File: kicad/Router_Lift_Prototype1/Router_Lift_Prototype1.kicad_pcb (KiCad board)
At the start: 2 copper layers, 143 x 93 mm, 37 parts, among them J1 Conn_01x02, J10 Conn_01x02, J11 Conn_01x04, J2 Conn_01x02, J3 Conn_01x06, J4 Conn_01x06, J5 Conn_01x06, J6 Conn_01x02, J7 Conn_01x02, J8 Conn_01x02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

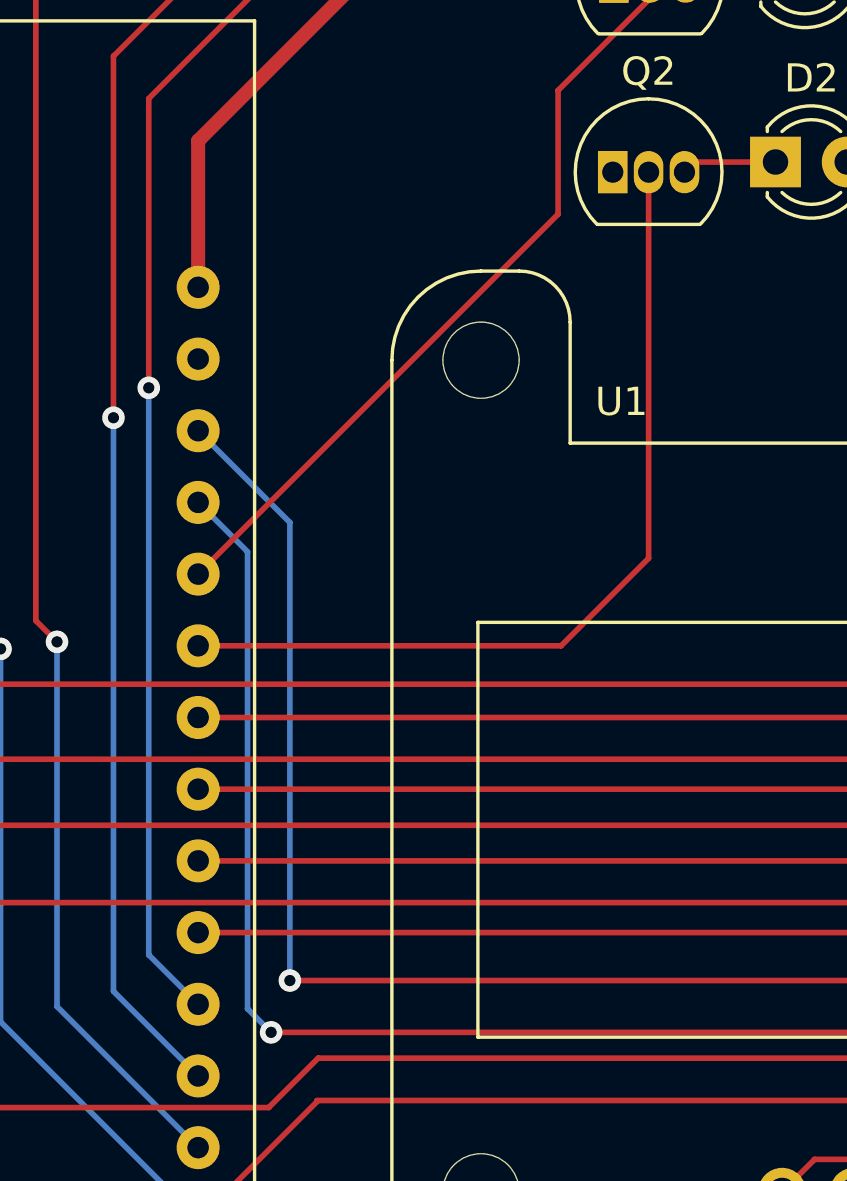
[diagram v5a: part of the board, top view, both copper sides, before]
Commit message: Created the board with DRV8711 Integration
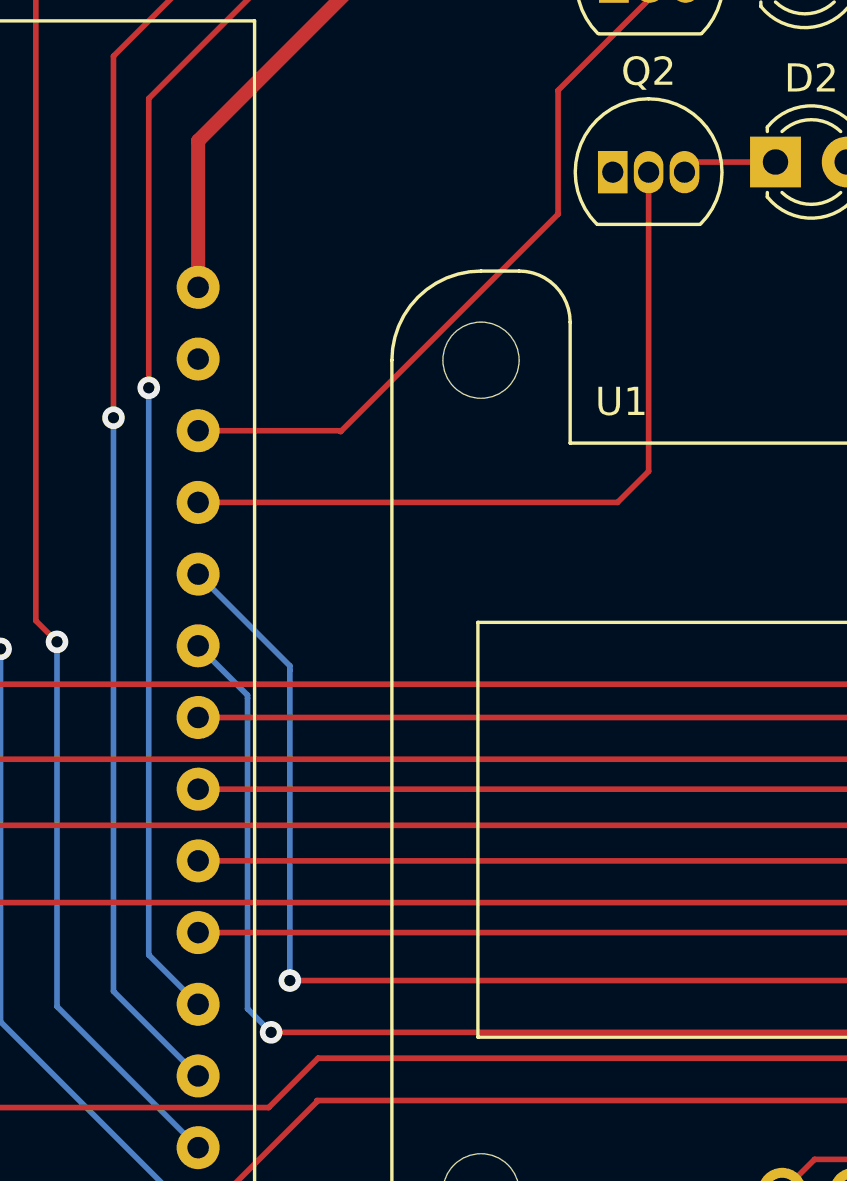
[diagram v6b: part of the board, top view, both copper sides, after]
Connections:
- U2 pad 10: /LED_GREEN -> /SLEEP
- U2 pad 11: /LED_RED -> /RESET
- U2 pad 12: /SLEEP -> /LED_GREEN
- U2 pad 13: /RESET -> /LED_RED
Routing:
- net /SLEEP: track 177.5 -> 172.5 mm
- net /RESET: track 170.6 -> 165.5 mm
- net /LED_GREEN: track 30.9 -> 27.0 mm
- net /LED_RED: track 27.6 -> 25.5 mm
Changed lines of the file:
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@@
     (grid_origin 50 143)
     (pcbplotparams
-      (layerselection 0x0001020_ffffffff)
+      (layerselection 0x00010e0_ffffffff)
       (disableapertmacros false)
       (usegerberextensions false)
@@
       (net 2 "/~{ENABLE}") (pinfunction "D26") (pintype "bidirectional"))
     (pad "10" thru_hole circle (at -12 3.86 180) (size 1.524 1.524) (drill 0.762) (layers *.Cu *.Mask)
-      (net 42 "/LED_GREEN") (pinfunction "D27") (pintype "bidirectional"))
+      (net 12 "/SLEEP") (pinfunction "D27") (pintype "bidirectional"))
     (pad "11" thru_hole circle (at -12 6.4 180) (size 1.524 1.524) (drill 0.762) (layers *.Cu *.Mask)
-      (net 41 "/LED_RED") (pinfunction "D14/HSPI-CLK") (pintype "bidirectional"))
+      (net 10 "/RESET") (pinfunction "D14/HSPI-CLK") (pintype "bidirectional"))
     (pad "12" thru_hole circle (at -12 8.94 180) (size 1.524 1.524) (drill 0.762) (layers *.Cu *.Mask)
-      (net 12 "/SLEEP") (pinfunction "D12/HSPI-MISO") (pintype "bidirectional"))
+      (net 42 "/LED_GREEN") (pinfunction "D12/HSPI-MISO") (pintype "bidirectional"))
     (pad "13" thru_hole circle (at -12 11.48 180) (size 1.524 1.524) (drill 0.762) (layers *.Cu *.Mask)
-      (net 10 "/RESET") (pinfunction "D13/HSPI-MOSI") (pintype "bidirectional"))
+      (net 41 "/LED_RED") (pinfunction "D13/HSPI-MOSI") (pintype "bidirectional"))
     (pad "14" thru_hole circle (at -12 14.02 180) (size 1.524 1.524) (drill 0.762) (layers *.Cu *.Mask)
       (net 1 "GND") (pinfunction "GND") (pintype "power_in"))
@@
   (segment (start 163.55 107) (end 142.75 107) (width 0.2) (layer "F.Cu") (net 10))
   (via (at 95.75 119.75) (size 0.8) (drill 0.4) (layers "F.Cu" "B.Cu") (net 10))
-  (segment (start 95.75 103.52) (end 92.5 100.27) (width 0.2) (layer "B.Cu") (net 10))
-  (segment (start 95.75 119.75) (end 95.75 103.52) (width 0.2) (layer "B.Cu") (net 10))
+  (segment (start 95.75 108.6) (end 95.75 108.75) (width 0.2) (layer "B.Cu") (net 10))
+  (segment (start 95.75 119.75) (end 95.75 108.75) (width 0.2) (layer "B.Cu") (net 10))
+  (segment (start 92.5 105.35) (end 95.75 108.6) (width 0.2) (layer "B.Cu") (net 10))
   (segment (start 154.34 121.19) (end 156.345 123.195) (width 0.2) (layer "F.Cu") (net 11))
   (segment (start 182 123.195) (end 156.345 123.195) (width 0.2) (layer "F.Cu") (net 11))
@@
   (segment (start 144.3 65.55) (end 149.11 65.55) (width 0.2) (layer "F.Cu") (net 12))
   (via (at 95.085 121.585) (size 0.8) (drill 0.4) (layers "F.Cu" "B.Cu") (net 12))
-  (segment (start 94.25 120.75) (end 94.25 104.56) (width 0.2) (layer "B.Cu") (net 12))
-  (segment (start 94.25 104.56) (end 92.5 102.81) (width 0.2) (layer "B.Cu") (net 12))
+  (segment (start 92.5 107.89) (end 94.25 109.64) (width 0.2) (layer "B.Cu") (net 12))
+  (segment (start 94.25 120.75) (end 94.25 109.75) (width 0.2) (layer "B.Cu") (net 12))
   (segment (start 95.085 121.585) (end 94.25 120.75) (width 0.2) (layer "B.Cu") (net 12))
+  (segment (start 94.25 109.64) (end 94.25 109.75) (width 0.2) (layer "B.Cu") (net 12))
   (segment (start 154.34 118.65) (end 160.08238 118.65) (width 0.5) (layer "F.Cu") (net 13))
   (segment (start 160.08238 118.65) (end 160.25 118.81762) (width 0.5) (layer "F.Cu") (net 13))
@@
   (segment (start 112.75 75.85) (end 117 71.6) (width 0.5) (layer "F.Cu") (net 40))
   (segment (start 108.5 84.964022) (end 108.5 84.36) (width 0.2) (layer "F.Cu") (net 41))
+  (segment (start 97.55 100.3) (end 105.25 92.6) (width 0.2) (layer "F.Cu") (net 41))
   (segment (start 105.25 92.6) (end 105.25 88.214022) (width 0.2) (layer "F.Cu") (net 41))
-  (segment (start 92.5 105.35) (end 105.25 92.6) (width 0.2) (layer "F.Cu") (net 41))
+  (segment (start 97.52 100.27) (end 97.55 100.3) (width 0.2) (layer "F.Cu") (net 41))
+  (segment (start 92.5 100.27) (end 97.52 100.27) (width 0.2) (layer "F.Cu") (net 41))
   (segment (start 105.25 88.214022) (end 108.5 84.964022) (width 0.2) (layer "F.Cu") (net 41))
-  (segment (start 92.5 107.89) (end 105.36 107.89) (width 0.2) (layer "F.Cu") (net 42))
-  (segment (start 105.36 107.89) (end 108.46 104.79) (width 0.2) (layer "F.Cu") (net 42))
-  (segment (start 108.46 104.79) (end 108.46 91.11) (width 0.2) (layer "F.Cu") (net 42))
+  (segment (start 108.46 101.71) (end 108.46 91.11) (width 0.2) (layer "F.Cu") (net 42))
+  (segment (start 92.5 102.81) (end 107.36 102.81) (width 0.2) (layer "F.Cu") (net 42))
+  (segment (start 107.36 102.81) (end 108.46 101.71) (width 0.2) (layer "F.Cu") (net 42))
   (segment (start 140.5 109.5) (end 144 113) (width 0.2) (layer "F.Cu") (net 44))
   (segment (start 144 113) (end 144 116.5) (width 0.2) (layer "F.Cu") (net 44))
